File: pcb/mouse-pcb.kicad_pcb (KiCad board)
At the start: 4 copper layers, 89.5 x 71.4 mm, 18 parts, among them J1 TYPE-C-31-M-12, SW1 D2FC-F-7N20M, SW2 D2FC-F-7N20M, SW3 D2FC-F-7N20M, U1 PAW3395-T6QU, U2 NRF52840-QIAA-R7

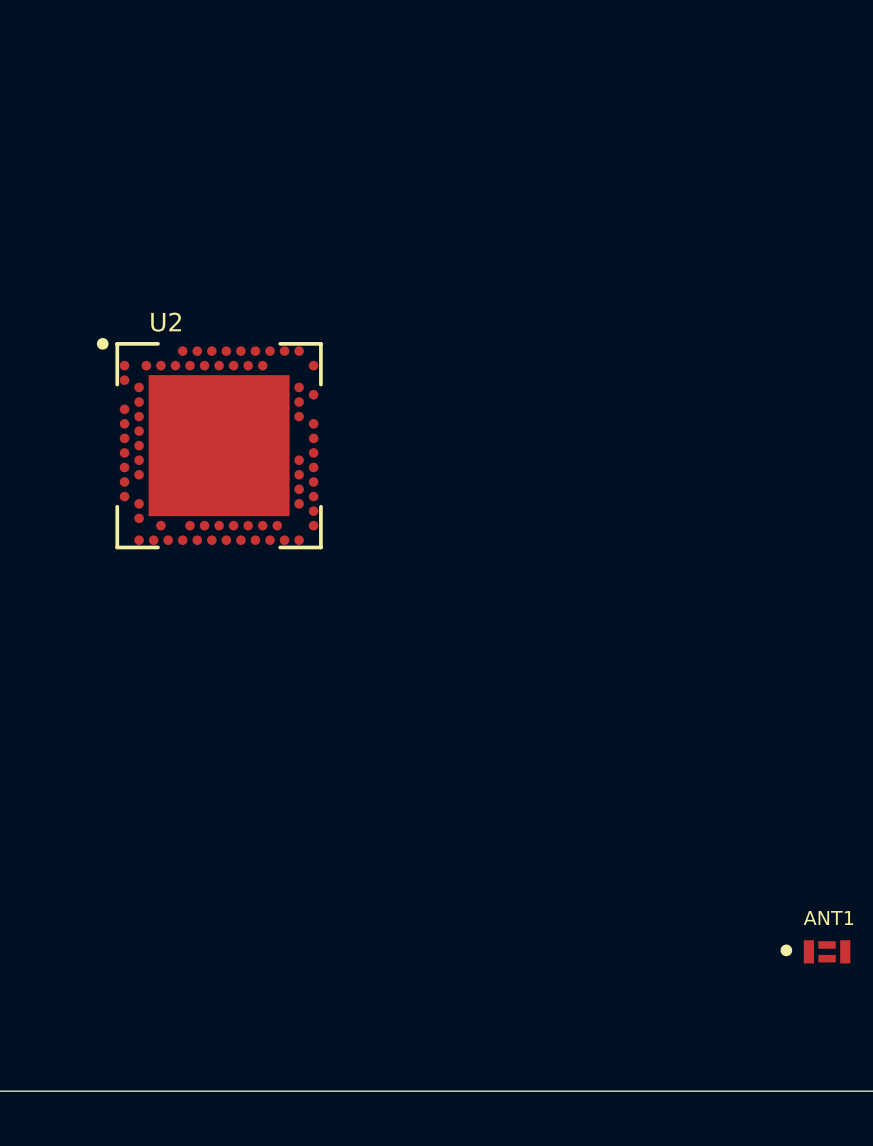
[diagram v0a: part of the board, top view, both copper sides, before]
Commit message: ci: ci implemented for kicad
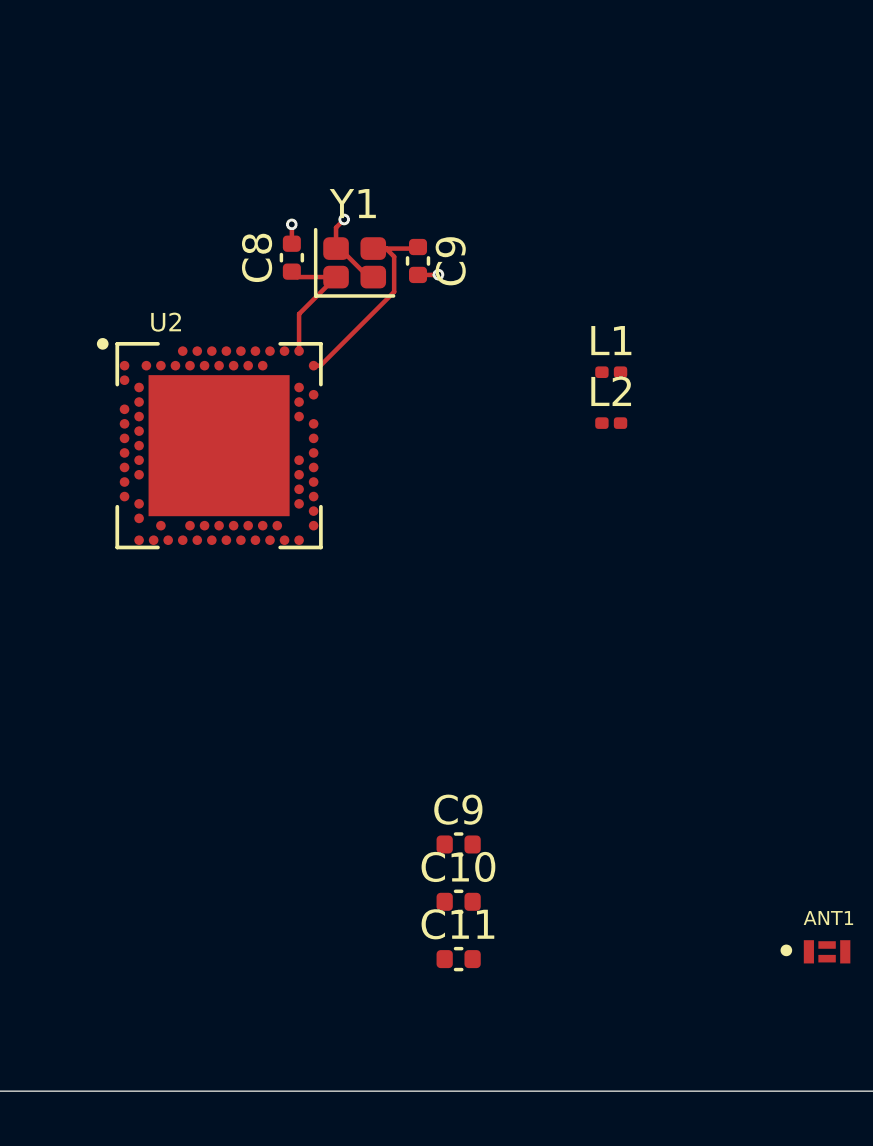
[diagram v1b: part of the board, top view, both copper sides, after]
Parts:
- added C10: 4.7uF, Capacitor_SMD:C_0402_1005Metric, F.Cu at (86.9, 94.5)
- added C11: 4.7uF, Capacitor_SMD:C_0402_1005Metric, F.Cu at (86.9, 96.4)
- added C8: 12pF, Capacitor_SMD:C_0402_1005Metric, F.Cu at (81.2, 72.3)
- added C9: 12pF, Capacitor_SMD:C_0402_1005Metric, F.Cu at (85.5, 72.4)
- added C9: 12pF, Capacitor_SMD:C_0402_1005Metric, F.Cu at (86.9, 92.5)
- added L1: 2nH, Inductor_SMD:L_0201_0603Metric, F.Cu at (92.2, 76.2)
- added L2: 3nH, Inductor_SMD:L_0201_0603Metric, F.Cu at (92.2, 78.0)
- added Y1: Crystal_GND24_Small, Crystal:Crystal_SMD_WE_IQXC-42-4Pin_2.0x1.6mm, F.Cu at (83.4, 72.5)
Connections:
- ANT1 pad 1: unconnected-(ANT1-RADIATOR_ELECTRODE-Pad1) -> RAD
- ANT1 pad 4: unconnected-(ANT1-FEEDING-Pad4) -> Net-(ANT1-FEEDING)
- U2 pad A23: unconnected-(U2C-XC2-PadA23) -> Net-(U2C-XC2)
- U2 pad AA24: unconnected-(U2C-SWDCLK-PadAA24) -> SWDCLK
- U2 pad AC13: unconnected-(U2A-P0.18/~{RESET}-PadAC13) -> RESET
- U2 pad AC24: unconnected-(U2C-SWDIO-PadAC24) -> SWDIO
- U2 pad AC5: unconnected-(U2B-DECUSB-PadAC5) -> DECUSB
- U2 pad AD2: unconnected-(U2B-VBUS-PadAD2) -> VBUS
- U2 pad AD4: unconnected-(U2A-D--PadAD4) -> D-
- U2 pad AD6: unconnected-(U2A-D+-PadAD6) -> D+
- U2 pad B24: unconnected-(U2C-XC1-PadB24) -> Net-(U2C-XC1)
- U2 pad B7: unconnected-(U2B-VSS-PadB7) -> GND
- U2 pad EXP: unconnected-(U2-PadEXP) -> GND
- U2 pad F23: unconnected-(U2B-VSS_PA-PadF23) -> GND
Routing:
- net Net-(U2C-XC1): track 0.00 -> 7.42 mm
- net Net-(U2C-XC2): track 0.00 -> 4.67 mm
- net GND: track 12.9 -> 17.1 mm, vias 8 -> 11

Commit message: feat: all micro circuits added
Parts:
- added C12: 4.7uF, Capacitor_SMD:C_0402_1005Metric, F.Cu at (73.2, 44.5)
- added C13: 1.0uF, Capacitor_SMD:C_0402_1005Metric, F.Cu at (73.2, 46.5)
- added C14: 100nF, Capacitor_SMD:C_0402_1005Metric, F.Cu at (73.2, 48.5)
- added C15: 100nF, Capacitor_SMD:C_0402_1005Metric, F.Cu at (76.0, 44.5)
- added C16: 100nF, Capacitor_SMD:C_0402_1005Metric, F.Cu at (76.0, 46.5)
- added C17: 4.7uF, Capacitor_SMD:C_0402_1005Metric, F.Cu at (76.0, 48.5)
- added C18: 1.0uF, Capacitor_SMD:C_0402_1005Metric, F.Cu at (78.9, 44.5)
- added C19: 47nF, Capacitor_SMD:C_0402_1005Metric, F.Cu at (78.9, 46.5)
- added C20: C, Capacitor_SMD:C_0402_1005Metric, F.Cu at (78.9, 48.5)
- added C21: 100nF, Capacitor_SMD:C_0402_1005Metric, F.Cu at (47.9, 68.0)
- added C22: 100pF, Capacitor_SMD:C_0402_1005Metric, F.Cu at (47.9, 70.0)
- added C23: 0.8pF, Capacitor_SMD:C_0402_1005Metric, F.Cu at (47.9, 71.9)
- added C24: 0.5pF, Capacitor_SMD:C_0402_1005Metric, F.Cu at (47.9, 73.9)
- added C25: 0.5pF, Capacitor_SMD:C_0402_1005Metric, F.Cu at (47.9, 75.9)
- added C26: 12pF, Capacitor_SMD:C_0402_1005Metric, F.Cu at (46.9, 56.8)
- added C27: 12pF, Capacitor_SMD:C_0402_1005Metric, F.Cu at (46.9, 58.8)
- added L3: 10uH, Inductor_SMD:L_0402_1005Metric, F.Cu at (70.3, 44.5)
- added L4: 10uH, Inductor_SMD:L_0402_1005Metric, F.Cu at (70.3, 46.5)
- added L5: 15nH, Inductor_SMD:L_0402_1005Metric, F.Cu at (70.3, 48.5)
- added L6: 4.7nH, Inductor_SMD:L_0201_0603Metric, F.Cu at (53.8, 77.0)
- added Y2: 32.768kHz, Crystal:Crystal_SMD_3215-2Pin_3.2x1.5mm, F.Cu at (48.0, 54.2)
- Y1: value Crystal_GND24_Small -> 32MHz
- moved L1 95.2 mm to (186.7, 87.0)
- moved L2 95.2 mm to (186.7, 88.8)
- moved ANT1 87.3 mm to (186.7, 101.7)
- moved C10 87.3 mm to (174.0, 100.0)
- moved C11 87.3 mm to (174.0, 102.0)
- moved C9 87.3 mm to (174.0, 98.0)
- moved G*** 69.1 mm to (90.5, 38.0)
- moved U2 44.9 mm to (123.5, 81.5), turned to 180 degrees
- moved C8 42.8 mm to (121.0, 88.0), turned to -90 degrees
- moved Y1 38.6 mm to (118.8, 87.8), turned to 180 degrees
- moved C9 34.7 mm to (116.7, 87.8), turned to 90 degrees
- moved R2 28.6 mm to (104.0, 76.1)
- moved C1 28.6 mm to (87.1, 81.4)
- moved C2 28.6 mm to (84.6, 81.4)
- moved C3 28.6 mm to (87.1, 85.6)
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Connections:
- U2 pad AB2: unconnected-(U2B-DCCH-PadAB2) -> DCCH
- U2 pad B3: unconnected-(U2B-DCC-PadB3) -> DCC
- U2 pad B5: unconnected-(U2B-DEC4-PadB5) -> DEC4
- U2 pad C1: unconnected-(U2B-DEC1-PadC1) -> DEC1
- U2 pad D2: unconnected-(U2A-P0.00/XL1-PadD2) -> Net-(U2A-P0.00/XL1)
- U2 pad D23: unconnected-(U2B-DEC3-PadD23) -> DEC3
- U2 pad E24: unconnected-(U2B-DEC6-PadE24) -> DEC4
- U2 pad F2: unconnected-(U2A-P0.01/XL2-PadF2) -> Net-(U2A-P0.01/XL2)
- U2 pad H23: unconnected-(U2A-ANT-PadH23) -> ANT_nrf
- U2 pad J24: unconnected-(U2A-P0.10/NFC2-PadJ24) -> MOTION
- U2 pad L24: unconnected-(U2A-P0.09/NFC1-PadL24) -> MISO
- U2 pad R1: unconnected-(U2A-P1.09-PadR1) -> NCS
- U2 pad R24: unconnected-(U2A-P1.06-PadR24) -> MOSI
- U2 pad U24: unconnected-(U2A-P1.04-PadU24) -> SCLK
- U2 pad W24: unconnected-(U2A-P1.02-PadW24) -> NRESET
- U2 pad Y2: unconnected-(U2B-VDDH-PadY2) -> VDDH

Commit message: feat: impedance calcualated
JLC04161H-3313(finished thicknes1.56mm+-10%
50 ohm 6.16 mil width (antenna)
90 ohm 4.4 mil width 4.0 mil spacing (differential pair)
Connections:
- U2 pad L24: MISO -> SCLK
- U2 pad U24: SCLK -> MISO
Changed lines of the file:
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@@
 			(layer "F.Mask"
 				(type "Top Solder Mask")
+				(color "Black")
 				(thickness 0.01)
 			)
@@
 			(layer "B.Mask"
 				(type "Bottom Solder Mask")
+				(color "Black")
 				(thickness 0.01)
 			)
@@
 			)
 			(copper_finish "None")
-			(dielectric_constraints no)
+			(dielectric_constraints yes)
 		)
 		(pad_to_mask_clearance 0)
@@
 		(capping no)
 		(filling no)
+		(zone_defaults)
 		(pcbplotparams
 			(layerselection 0x00000000_00000000_55555555_5755f5ff)
@@
 			(size 0.33 0.33)
 			(layers "F.Cu" "F.Mask" "F.Paste")
-			(net "MISO")
+			(net "SCLK")
 			(pinfunction "P0.09/NFC1_L24")
 			(pintype "bidirectional")
@@
 			(size 0.33 0.33)
 			(layers "F.Cu" "F.Mask" "F.Paste")
-			(net "SCLK")
+			(net "MISO")
 			(pinfunction "P1.04_U24")
 			(pintype "bidirectional")
@@
 	)
 	(segment
+		(start 100.7 86.57)
+		(end 108.725 86.57)
+		(width 0.156)
+		(layer "F.Cu")
+		(net "MOTION")
+	)
+	(segment
 		(start 103.27 81.23)
 		(end 103.605 80.895)
@@
 	)
 	(segment
-		(start 100.895 76.085)
-		(end 100.7 75.89)
-		(width 0.5)
-		(layer "F.Cu")
-		(net "Net-(U1-LED_P)")
-	)
-	(segment
-		(start 101.065 76.085)
-		(end 100.895 76.085)
+		(start 101.145 79.895)
+		(end 109.05 79.895)
 		(width 0.156)
 		(layer "F.Cu")
-		(net "Net-(U1-LED_P)")
+		(net "NCS")
 	)
 	(segment
-		(start 102.97 76.085)
-		(end 100.895 76.085)
-		(width 0.5)
+		(start 100.7 79.45)
+		(end 101.145 79.895)
+		(width 0.156)
 		(layer "F.Cu")
-		(net "Net-(U1-LED_P)")
+		(net "NCS")
 	)
 	(segment
-		(start 89.98 80.36)
-		(end 90 80.34)
-		(width 0.5)
+		(start 100.7 83.01)
+		(end 108.99 83.01)
+		(width 0.156)
 		(layer "F.Cu")
-		(net "VDDREG")
+		(net "MOSI")
 	)
 	(segment
-		(start 87.095 80.36)
-		(end 89.98 80.36)
-		(width 0.5)
+		(start 108.99 83.01)
+		(end 109.05 83.07)
+		(width 0.156)
 		(layer "F.Cu")
-		(net "VDDREG")
+		(net "MOSI")
 	)
 	(segment
-		(start 84.937531 80.36)
-		(end 87.095 80.36)
-		(width 0.5)
+		(start 100.7 84.79)
+		(end 108.865 84.79)
+		(width 0.156)
 		(layer "F.Cu")
-		(net "VDDREG")
+		(net "SCLK")
 	)
 	(segment
-		(start 100.7 86.57)
-		(end 108.725 86.57)
+		(start 108.735 77.67)
+		(end 109.05 77.355)
 		(width 0.156)
 		(layer "F.Cu")
-		(net "MOTION")
+		(net "NRESET")
 	)
 	(segment
-		(start 100.7 84.79)
-		(end 108.865 84.79)
+		(start 100.7 77.67)
+		(end 108.735 77.67)
 		(width 0.156)
 		(layer "F.Cu")
-		(net "SCLK")
+		(net "NRESET")
 	)
 	(segment
-		(start 100.7 83.01)
-		(end 108.99 83.01)
-		(width 0.156)
+		(start 100.895 76.085)
+		(end 100.7 75.89)
+		(width 0.5)
 		(layer "F.Cu")
-		(net "MOSI")
+		(net "Net-(U1-LED_P)")
 	)
 	(segment
-		(start 108.99 83.01)
-		(end 109.05 83.07)
+		(start 101.065 76.085)
+		(end 100.895 76.085)
 		(width 0.156)
 		(layer "F.Cu")
-		(net "MOSI")
+		(net "Net-(U1-LED_P)")
 	)
 	(segment
-		(start 101.145 79.895)
-		(end 109.05 79.895)
-		(width 0.156)
+		(start 102.97 76.085)
+		(end 100.895 76.085)
+		(width 0.5)
 		(layer "F.Cu")
-		(net "NCS")
+		(net "Net-(U1-LED_P)")
 	)
 	(segment
-		(start 100.7 79.45)
-		(end 101.145 79.895)
-		(width 0.156)
+		(start 89.98 80.36)
+		(end 90 80.34)
+		(width 0.5)
 		(layer "F.Cu")
-		(net "NCS")
+		(net "VDDREG")
 	)
 	(segment
-		(start 108.735 77.67)
-		(end 109.05 77.355)
-		(width 0.156)
+		(start 87.095 80.36)
+		(end 89.98 80.36)
+		(width 0.5)
 		(layer "F.Cu")
-		(net "NRESET")
+		(net "VDDREG")
 	)
 	(segment
-		(start 100.7 77.67)
-		(end 108.735 77.67)
-		(width 0.156)
+		(start 84.937531 80.36)
+		(end 87.095 80.36)
+		(width 0.5)
 		(layer "F.Cu")
-		(net "NRESET")
+		(net "VDDREG")
 	)
 	(zone
